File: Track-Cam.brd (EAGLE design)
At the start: 65 x 56 mm, 40 parts, among them IC1 STM32F042KT/M, IC2 BD6211F/M, IC3 BD6211F/M, X1 RASPI_BOARD_B+#_HC

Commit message: fix some bug
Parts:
- C4, C5: value 20p -> 22p; device gen-discrete:SMD2012 -> gen-discrete:SMD1608
- R1: value 1M -> 300K; device gen-discrete:SMD1608 -> gen-discrete:SMD2012
- R2: device generic:SMD1608 -> gen-discrete:SMD2012
- R3: value 330 -> 300
- R4: value 330 -> 100
- R5: value 330 -> 470
- moved C4 2.29 mm to (13.3, 43.8)
- moved C5 1.80 mm to (13.3, 41.3)
- moved R1 1.42 mm to (26.7, 41.9), turned to 0 degrees
- moved C1 0.63 mm to (29.8, 45.7)
- moved XT1 0.63 mm to (20.3, 43.2)
- renumbered X1 to P1
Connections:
- new net N$1: C5.2, R1.1, XT1.2
- net OSC_IN: no longer R1.1
- net OSC_OUT: no longer C5.2, XT1.2
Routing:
- net VDD: track 51.8 -> 12.5 mm
- net GND: track 198.2 -> 174.9 mm, vias 107 -> 108
- net OSC_OUT: track 18.6 -> 5.19 mm
- net N$1: track 0.00 -> 12.3 mm
- net SDA: track 35.0 -> 32.4 mm
- net +3V3: vias 19 -> 15

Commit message: optimize wiring
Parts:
- added R6, R7, R8, R9: 10K, gen-discrete:SMD2012
- U$1: value PRODUCT-LOGO-TRACKCAM -> (none); device logo:TRACKCAM-LOGO -> logo:OPIOPAN-LOGO
- U$2: value OPIOPAN-LOGO -> (none); device logo:OPIOPAN-LOGO -> logo:TRACKCAM-LOGO
- moved U$2 18.7 mm to (0.64, 32.1)
- moved U$1 17.1 mm to (0.95, 14.0)
- moved R2 0.63 mm to (33.3, 47.9)
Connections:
- net GND: now also R6.2, R7.2, R8.2, R9.2
- net MOTOR1_F: now also R6.1
- net MOTOR1_R: now also R7.1
- net MOTOR2_F: now also R8.1
- net MOTOR2_R: now also R9.1
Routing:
- net MOTOR2_R: track 45.2 -> 61.1 mm, vias 0 -> 1
- net MOTOR2_F: track 54.1 -> 57.8 mm, vias 2 -> 1
- net MOTOR1_R: track 26.3 -> 28.6 mm, vias 0 -> 1
- net MOTOR1_F: track 36.5 -> 38.3 mm, vias 0 -> 1
- net BOOT0: track 3.73 -> 3.10 mm
- net GND: track 174.9 -> 174.8 mm, vias 108 -> 135

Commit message: fix some wiring bug
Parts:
- moved C9 1.27 mm to (55.2, 11.4)
- moved C8 0.63 mm to (55.9, 24.8)
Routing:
- net GND: track 174.8 -> 123.2 mm, vias 135 -> 78
- net MOTOR2_R: track 61.1 -> 47.5 mm
- net +5V: track 34.8 -> 21.1 mm
- net MOTOR2_F: track 57.8 -> 56.5 mm, vias 1 -> 3
- net MOTOR1-: track 14.2 -> 14.8 mm

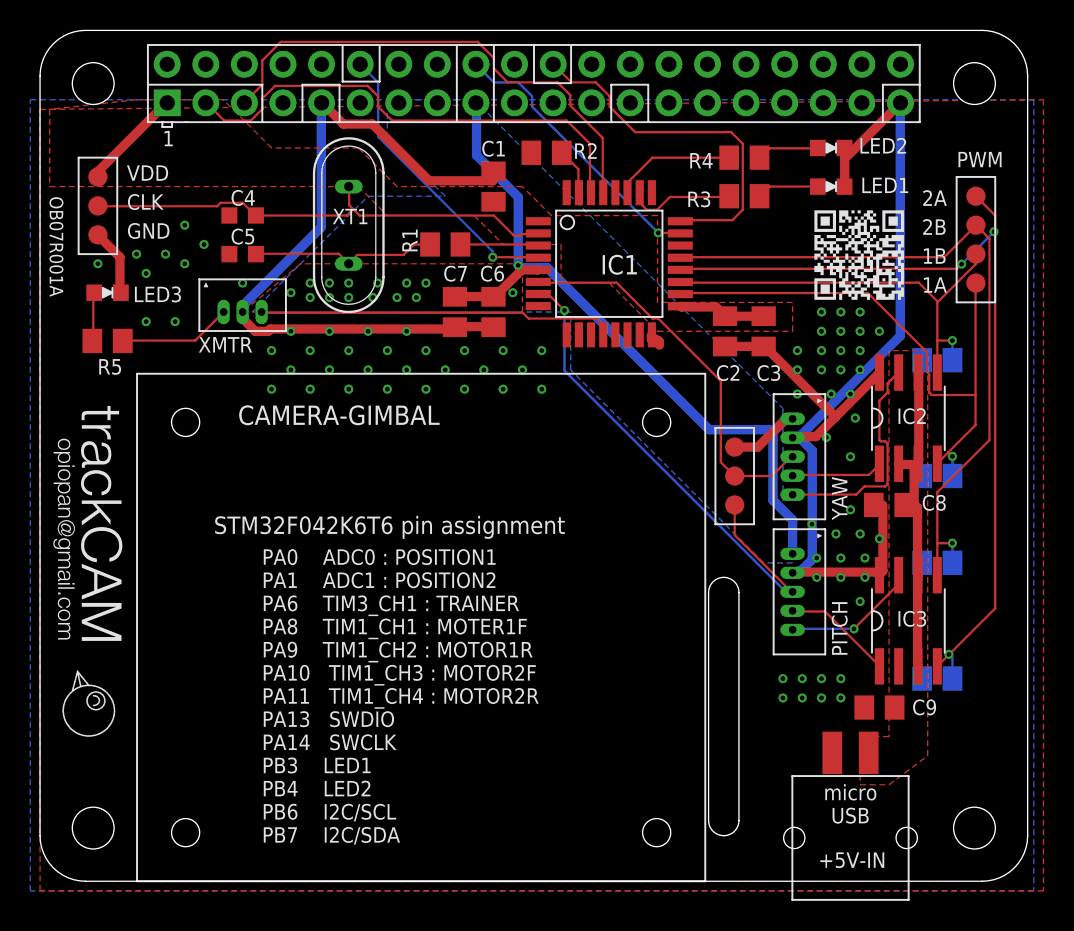
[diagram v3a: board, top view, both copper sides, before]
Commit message: fix 5v line bug
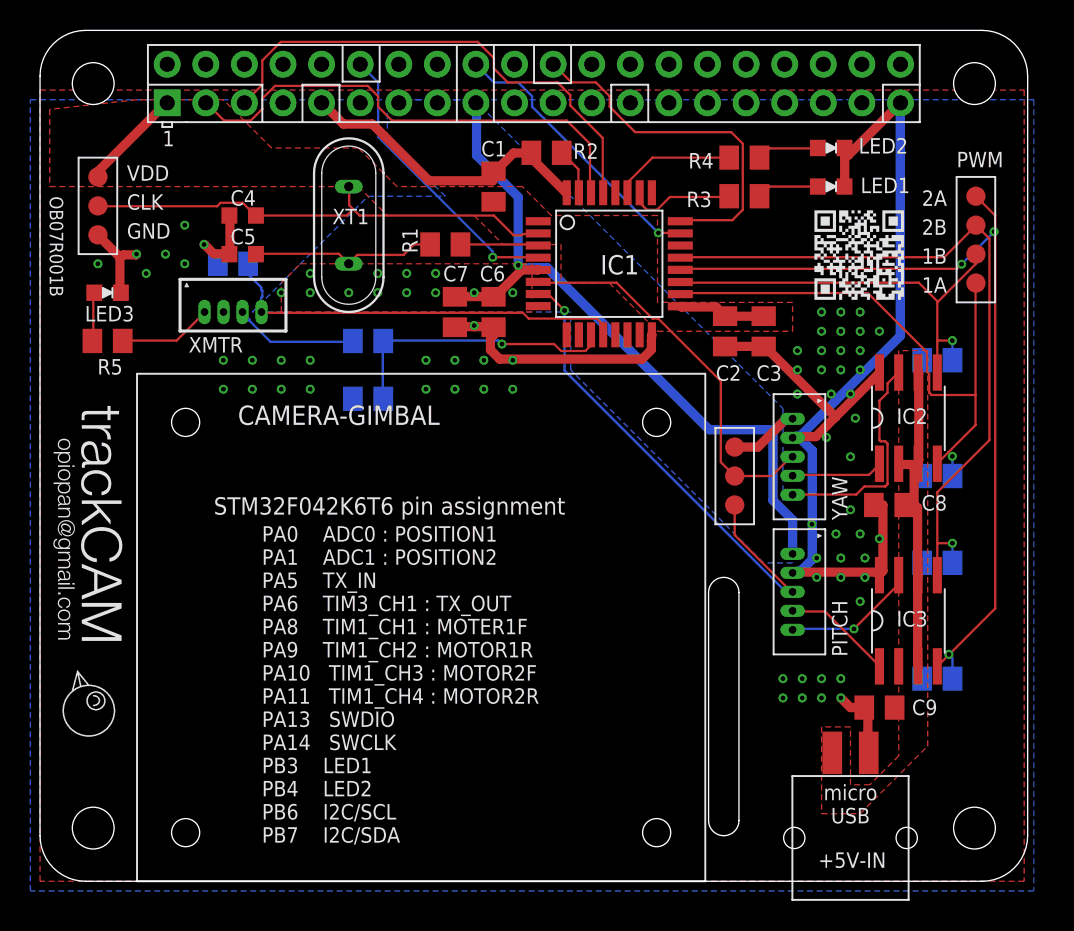
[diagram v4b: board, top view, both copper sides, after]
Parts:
- added R10: 2.2K, gen-discrete:SMD2012
- added R11: 3.3K, gen-discrete:SMD2012
- added R12: 10K, gen-discrete:SMD2012
- XMTR: value 53047-0310 -> 53047-0410; device connector:53047-0310 -> connector:53047-0410
- moved XMTR 0.64 mm to (12.7, 37.5)
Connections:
- removed net TRAINER: IC1.12, XMTR.3
- new net TX_IN: IC1.11, R10.2, R11.1
- new net TX_IN_5V: R10.1, XMTR.3
- new net TX_OUT: IC1.12, R12.1, XMTR.4
- net GND: now also R11.2, R12.2
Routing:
- net TX_OUT: track 0.00 -> 27.1 mm
- net TRAINER: track 23.5 -> 0.00 mm
- net TX_IN: track 0.00 -> 18.7 mm, vias 0 -> 1
- net TX_IN_5V: track 0.00 -> 8.21 mm
- net N$10: track 7.43 -> 6.19 mm
- net GND: track 123.2 -> 123.9 mm, vias 78 -> 65
- net +3V3: vias 15 -> 13
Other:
- board text added: "OB07R001B"
- board text added: "PA0 ADC0 : POSITION1 PA1 ADC1 : POSITION2 PA5 TX_IN PA6 TIM3_CH1 : TX_OUT PA8 TIM1_CH1 : MOTER1F PA9 TIM1_CH2 : MOTOR1R PA10 TIM1_CH3 : MOTOR2F PA11 TIM1_CH4 : MOTOR2R PA13 SWDIO PA14 SWCLK PB3 LED1 PB4 LED2 PB6 I2C/SCL PB7 I2C/SDA"
- board text removed: "OB07R001A"
- board text removed: "PA0 ADC0 : POSITION1 PA1 ADC1 : POSITION2 PA6 TIM3_CH1 : TRAINER PA8 TIM1_CH1 : MOTER1F PA9 TIM1_CH2 : MOTOR1R PA10 TIM1_CH3 : MOTOR2F PA11 TIM1_CH4 : MOTOR2R PA13 SWDIO PA14 SWCLK PB3 LED1 PB4 LED2 PB6 I2C/SCL PB7 I2C/SDA"

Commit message: fix BOM for 1st production
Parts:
- R1: value 300K -> 100
- R3: value 300 -> 100
- R4: value 100 -> 330
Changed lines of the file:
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@@
 <attribute name="NAME" x="20.447" y="43.2435" size="1.016" layer="25" font="vector" align="bottom-center"/>
 </element>
-<element name="R1" library="gen-discrete" package="SMD2012" value="300K" x="26.67" y="41.91" smashed="yes">
+<element name="R1" library="gen-discrete" package="SMD2012" value="100" x="26.67" y="41.91" smashed="yes">
 <attribute name="NAME" x="23.838" y="43.0045" size="1.016" layer="25" font="vector" rot="R270"/>
 <attribute name="VALUE" x="25.87" y="40.26" size="1.016" layer="27"/>
@@
 <attribute name="VALUE" x="51.27" y="46.56" size="1.016" layer="27"/>
 </element>
-<element name="R3" library="gen-discrete" package="SMD2012" value="300" x="46.355" y="45.085" smashed="yes">
+<element name="R3" library="gen-discrete" package="SMD2012" value="100" x="46.355" y="45.085" smashed="yes">
 <attribute name="NAME" x="44.212" y="44.3725" size="1.016" layer="25" font="vector" align="bottom-right"/>
 <attribute name="VALUE" x="45.355" y="43.185" size="1.016" layer="27" font="vector"/>
 </element>
-<element name="R4" library="gen-discrete" package="SMD2012" value="100" x="46.355" y="47.625" smashed="yes">
+<element name="R4" library="gen-discrete" package="SMD2012" value="330" x="46.355" y="47.625" smashed="yes">
 <attribute name="NAME" x="44.339" y="46.9125" size="1.016" layer="25" font="vector" align="bottom-right"/>
 <attribute name="VALUE" x="45.355" y="45.725" size="1.016" layer="27" font="vector"/>
